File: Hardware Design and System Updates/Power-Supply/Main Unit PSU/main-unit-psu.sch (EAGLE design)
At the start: 13 parts, among them U1 BA033CC0FP-E2TO252-3_ROM, U2 BA033CC0FP-E2TO252-3_ROM

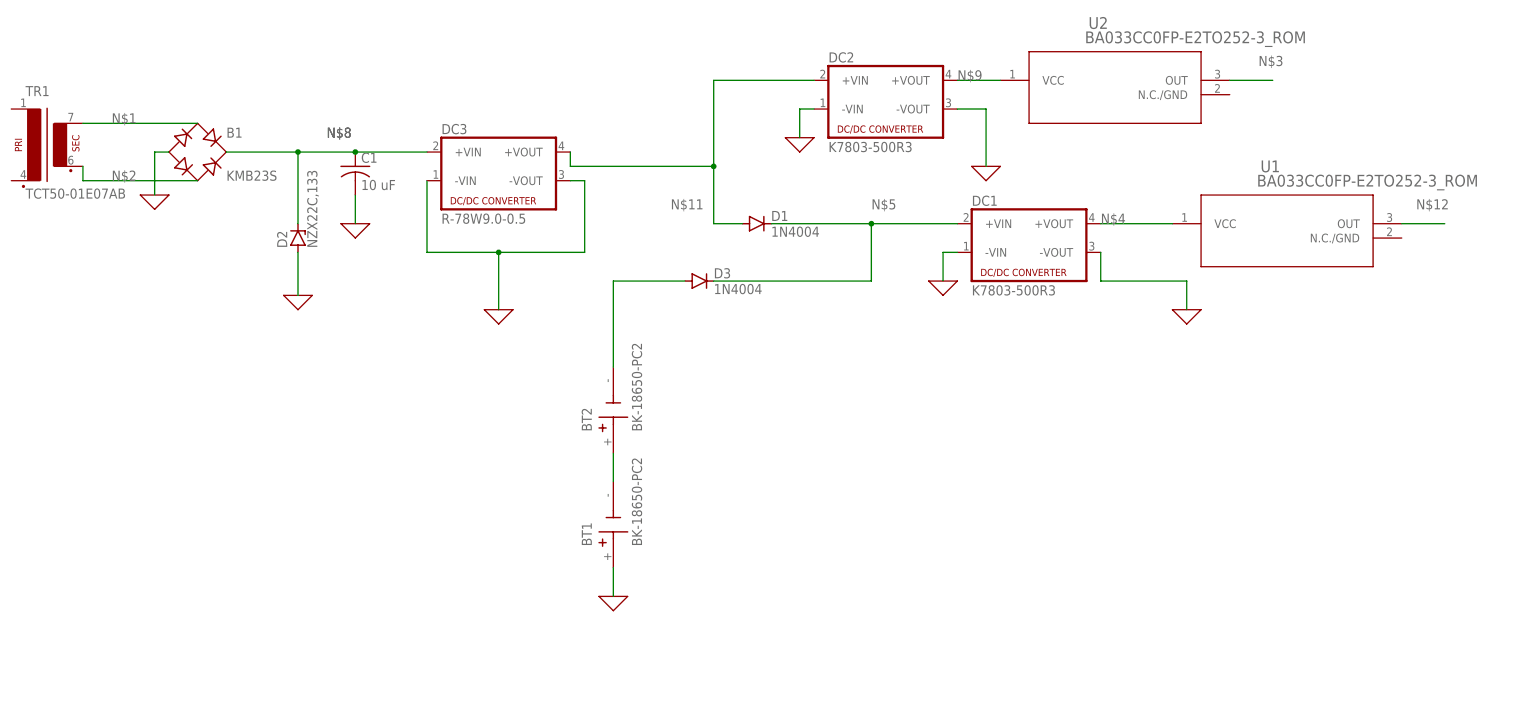
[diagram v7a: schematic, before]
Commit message: Finished BOM,analysis and diagrams for PSUs
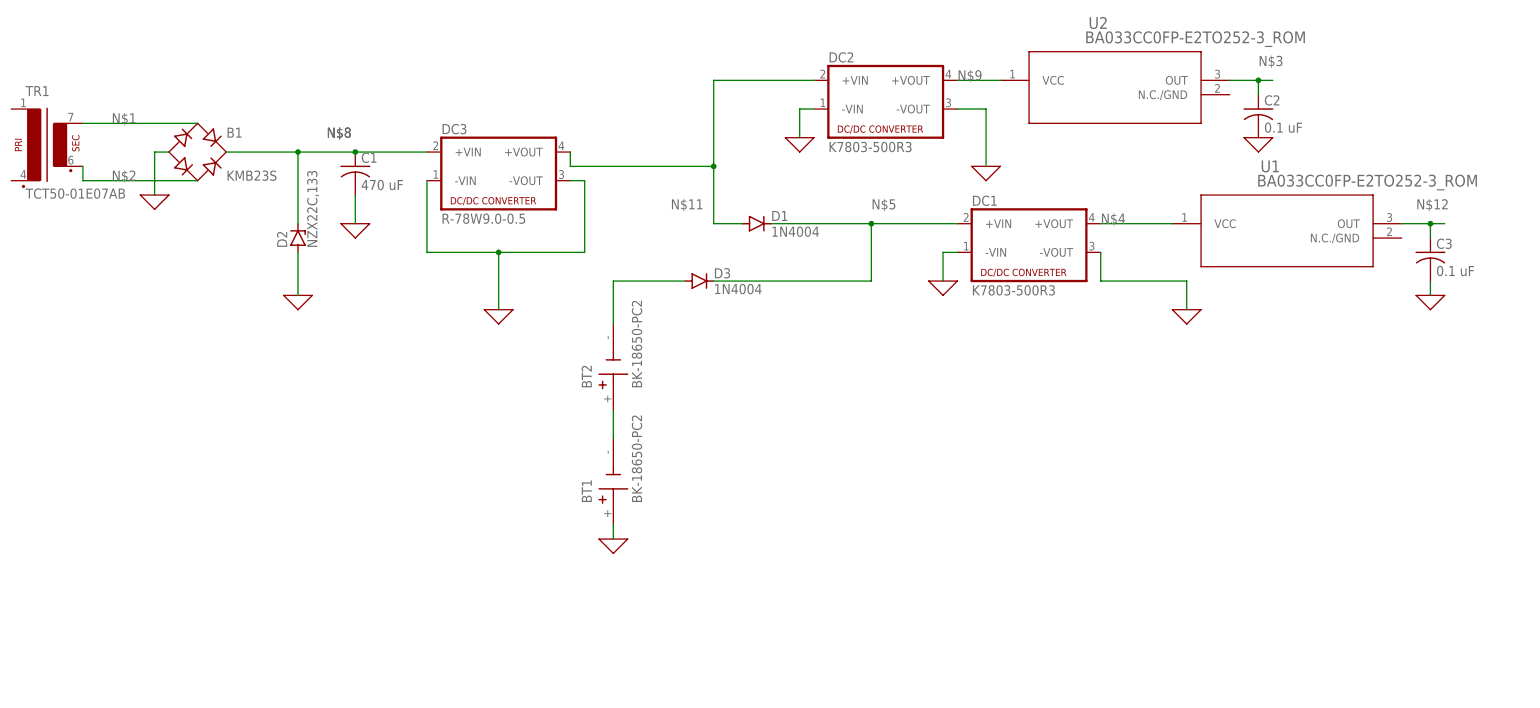
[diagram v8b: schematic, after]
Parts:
- added C2, C3: 0.1 uF, rcl:C-US050-024X044
- C1: value 10 uF -> 470 uF
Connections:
- net 0: now also C2.2, C3.2
- net N$12: now also C3.1
- net N$3: now also C2.1
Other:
- moved on the sheet: BT1, BT2
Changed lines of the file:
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@@
 <parts>
 <part name="D1" library="diode" library_urn="urn:adsk.eagle:library:210" deviceset="1N4004" device="" package3d_urn="urn:adsk.eagle:package:43336/1"/>
-<part name="C1" library="rcl" library_urn="urn:adsk.eagle:library:334" deviceset="C-US" device="050-024X044" package3d_urn="urn:adsk.eagle:package:23643/1" value="10 uF"/>
+<part name="C1" library="rcl" library_urn="urn:adsk.eagle:library:334" deviceset="C-US" device="050-024X044" package3d_urn="urn:adsk.eagle:package:23643/1" value="470 uF"/>
 <part name="B1" library="rectifier" library_urn="urn:adsk.eagle:library:336" deviceset="B-DIL" device="" package3d_urn="urn:adsk.eagle:package:23868/1" value="KMB23S"/>
 <part name="X_1" library="ngspice-simulation" library_urn="urn:adsk.eagle:library:527439" deviceset="GND" device=""/>
@@
 <part name="BT2" library="BK-18650-PC2" deviceset="BK-18650-PC2" device=""/>
 <part name="D3" library="diode" library_urn="urn:adsk.eagle:library:210" deviceset="1N4004" device="" package3d_urn="urn:adsk.eagle:package:43336/1"/>
+<part name="C2" library="rcl" library_urn="urn:adsk.eagle:library:334" deviceset="C-US" device="050-024X044" package3d_urn="urn:adsk.eagle:package:23643/1" value="0.1 uF"/>
+<part name="C3" library="rcl" library_urn="urn:adsk.eagle:library:334" deviceset="C-US" device="050-024X044" package3d_urn="urn:adsk.eagle:package:23643/1" value="0.1 uF"/>
+<part name="X_10" library="ngspice-simulation" library_urn="urn:adsk.eagle:library:527439" deviceset="GND" device=""/>
+<part name="X_11" library="ngspice-simulation" library_urn="urn:adsk.eagle:library:527439" deviceset="GND" device=""/>
 </parts>
 <sheets>
@@
 </instance>
 <instance part="X_6" gate="G$1" x="83.82" y="71.12" smashed="yes"/>
-<instance part="BT1" gate="G$1" x="50.8" y="2.54" smashed="yes" rot="R90">
-<attribute name="NAME" x="46.99" y="-1.27" size="1.778" layer="95" rot="R90"/>
-<attribute name="VALUE" x="55.88" y="-1.27" size="1.778" layer="96" rot="R90"/>
-</instance>
-<instance part="X_5" gate="G$1" x="50.8" y="-10.16" smashed="yes"/>
+<instance part="BT1" gate="G$1" x="50.8" y="10.16" smashed="yes" rot="R90">
+<attribute name="NAME" x="46.99" y="6.35" size="1.778" layer="95" rot="R90"/>
+<attribute name="VALUE" x="55.88" y="6.35" size="1.778" layer="96" rot="R90"/>
+</instance>
+<instance part="X_5" gate="G$1" x="50.8" y="0" smashed="yes"/>
 <instance part="DC3" gate="G$1" x="30.48" y="66.04" smashed="yes">
 <attribute name="NAME" x="20.32" y="71.755" size="1.778" layer="95"/>
@@
 <attribute name="VALUE" x="134.3352" y="87.8586" size="2.083" layer="96" ratio="6"/>
 </instance>
-<instance part="BT2" gate="G$1" x="50.8" y="22.86" smashed="yes" rot="R90">
-<attribute name="NAME" x="46.99" y="19.05" size="1.778" layer="95" rot="R90"/>
-<attribute name="VALUE" x="55.88" y="19.05" size="1.778" layer="96" rot="R90"/>
+<instance part="BT2" gate="G$1" x="50.8" y="30.48" smashed="yes" rot="R90">
+<attribute name="NAME" x="46.99" y="26.67" size="1.778" layer="95" rot="R90"/>
+<attribute name="VALUE" x="55.88" y="26.67" size="1.778" layer="96" rot="R90"/>
 </instance>
 <instance part="D3" gate="1" x="66.04" y="45.72" smashed="yes">
@@
 <attribute name="VALUE" x="68.58" y="43.4086" size="1.778" layer="96"/>
 </instance>
+<instance part="C2" gate="G$1" x="165.1" y="76.2" smashed="yes">
+<attribute name="NAME" x="166.116" y="76.835" size="1.778" layer="95"/>
+<attribute name="VALUE" x="166.116" y="72.009" size="1.778" layer="96"/>
+</instance>
+<instance part="C3" gate="G$1" x="195.58" y="50.8" smashed="yes">
+<attribute name="NAME" x="196.596" y="51.435" size="1.778" layer="95"/>
+<attribute name="VALUE" x="196.596" y="46.609" size="1.778" layer="96"/>
+</instance>
+<instance part="X_10" gate="G$1" x="195.58" y="43.18" smashed="yes"/>
+<instance part="X_11" gate="G$1" x="165.1" y="71.12" smashed="yes"/>
 </instances>
 <busses>
@@
 <pinref part="X_5" gate="G$1" pin="0"/>
 <pinref part="BT1" gate="G$1" pin="+"/>
-<wire x1="50.8" y1="-10.16" x2="50.8" y2="-5.08" width="0.1524" layer="91"/>
+<wire x1="50.8" y1="0" x2="50.8" y2="2.54" width="0.1524" layer="91"/>
 </segment>
 <segment>
@@
 <pinref part="DC2" gate="G$1" pin="-VOUT"/>
 <wire x1="116.84" y1="76.2" x2="111.76" y2="76.2" width="0.1524" layer="91"/>
+</segment>
+<segment>
+<pinref part="C2" gate="G$1" pin="2"/>
+<pinref part="X_11" gate="G$1" pin="0"/>
+</segment>
+<segment>
+<pinref part="X_10" gate="G$1" pin="0"/>
+<pinref part="C3" gate="G$1" pin="2"/>
+<wire x1="195.58" y1="43.18" x2="195.58" y2="45.72" width="0.1524" layer="91"/>
 </segment>
 </net>
@@
 <net name="N$3" class="0">
 <segment>
-<wire x1="160.02" y1="81.28" x2="167.64" y2="81.28" width="0.1524" layer="91"/>
+<wire x1="160.02" y1="81.28" x2="165.1" y2="81.28" width="0.1524" layer="91"/>
 <label x="165.1" y="83.82" size="1.778" layer="95"/>
 <pinref part="U2" gate="A" pin="OUT"/>
+<pinref part="C2" gate="G$1" pin="1"/>
+<wire x1="165.1" y1="81.28" x2="167.64" y2="81.28" width="0.1524" layer="91"/>
+<wire x1="165.1" y1="78.74" x2="165.1" y2="81.28" width="0.1524" layer="91"/>
+<junction x="165.1" y="81.28"/>
 </segment>
 </net>
 <net name="N$12" class="0">
 <segment>
-<wire x1="190.5" y1="55.88" x2="198.12" y2="55.88" width="0.1524" layer="91"/>
+<wire x1="190.5" y1="55.88" x2="195.58" y2="55.88" width="0.1524" layer="91"/>
 <label x="193.04" y="58.42" size="1.778" layer="95"/>
 <pinref part="U1" gate="A" pin="OUT"/>
+<pinref part="C3" gate="G$1" pin="1"/>
+<wire x1="195.58" y1="55.88" x2="198.12" y2="55.88" width="0.1524" layer="91"/>
+<wire x1="195.58" y1="53.34" x2="195.58" y2="55.88" width="0.1524" layer="91"/>
+<junction x="195.58" y="55.88"/>
 </segment>
 </net>
@@
 <pinref part="BT2" gate="G$1" pin="+"/>
 <pinref part="BT1" gate="G$1" pin="-"/>
-<wire x1="50.8" y1="10.16" x2="50.8" y2="15.24" width="0.1524" layer="91"/>
+<wire x1="50.8" y1="17.78" x2="50.8" y2="22.86" width="0.1524" layer="91"/>
 </segment>
 </net>
@@
 <segment>
 <pinref part="BT2" gate="G$1" pin="-"/>
-<wire x1="50.8" y1="30.48" x2="50.8" y2="45.72" width="0.1524" layer="91"/>
+<wire x1="50.8" y1="38.1" x2="50.8" y2="45.72" width="0.1524" layer="91"/>
 <wire x1="63.5" y1="45.72" x2="50.8" y2="45.72" width="0.1524" layer="91"/>
 <pinref part="D3" gate="1" pin="A"/>
